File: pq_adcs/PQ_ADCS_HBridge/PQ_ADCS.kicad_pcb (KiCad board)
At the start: 6 copper layers, 40 x 40 mm, 53 parts, among them J1 CES-110-02-L-S, J10 Pico-Clasp_01x09, J11 Pico-Clasp_01x15, J12 CES-102-02-L-S, J2 CES-110-02-L-S, J3 CES-110-02-L-S, J4 CES-110-02-L-S, J5 Pico-Clasp_01x03, J6 Pico-Clasp_01x10, J7 Pico-Clasp_01x10, J8 Pico-Clasp_01x10, J9 Pico-Clasp_01x10, U1 LPV542, U2 LPV542, U3 LPV542, U4 IIM-42652, U5 DRV8214RTER, U6 TMUX1108RSVR, U7 MMC5983MA, U8 DRV8214RTER, U9 DRV8214RTER

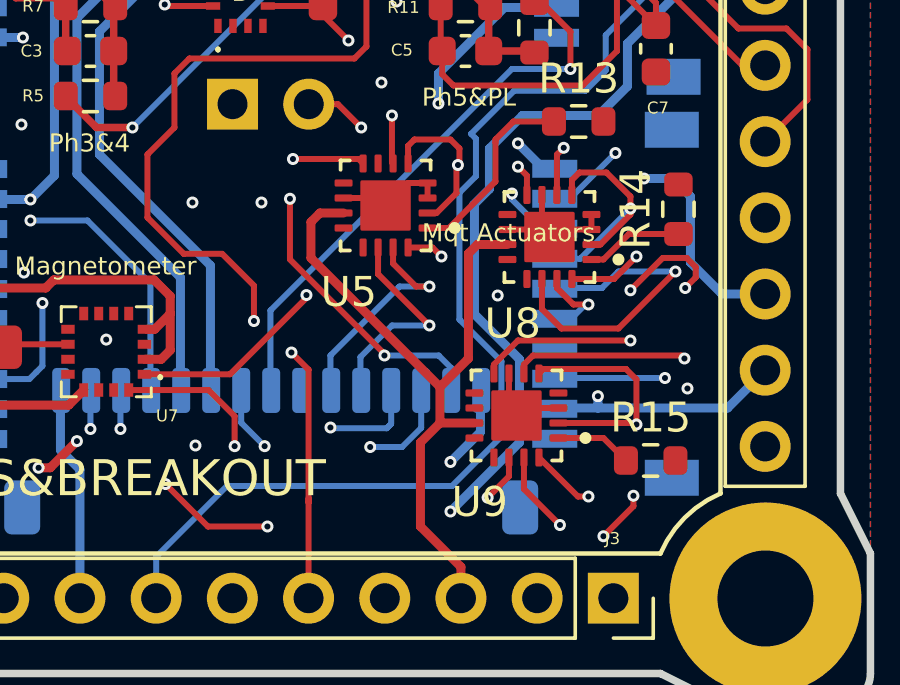
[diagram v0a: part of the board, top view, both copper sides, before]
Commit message: NC digital pincs fix
Unused digital pins as well as I2C pins are now set as not connected instead of grounded. Added lock files to gitignore
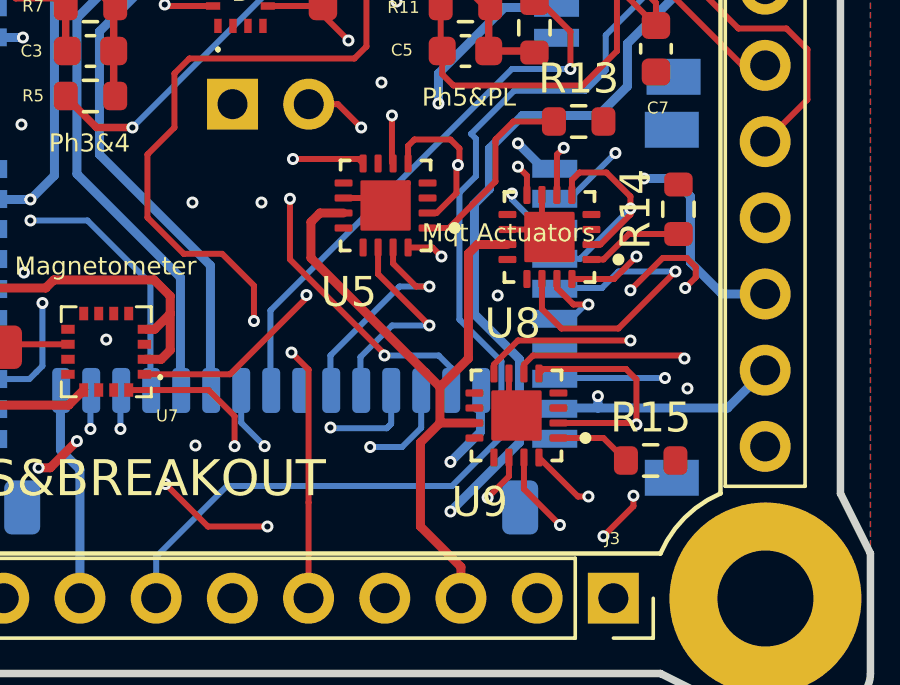
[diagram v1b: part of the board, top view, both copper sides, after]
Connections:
- U5 pad 3: GND -> unconnected-(U5-RC_OUT-Pad3)
- U5 pad 4: GND -> unconnected-(U5-~{FAULT}-Pad4)
- U8 pad 3: GND -> unconnected-(U8-RC_OUT-Pad3)
- U8 pad 4: GND -> unconnected-(U8-~{FAULT}-Pad4)
- U9 pad 3: GND -> unconnected-(U9-RC_OUT-Pad3)
- U9 pad 4: GND -> unconnected-(U9-~{FAULT}-Pad4)
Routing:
- net GND: track 20.2 -> 16.3 mm
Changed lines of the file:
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@@
 	(net 79 "unconnected-(U9-A1-Pad9)")
 	(net 80 "/PHT6_ADCS")
+	(net 81 "unconnected-(U5-~{FAULT}-Pad4)")
+	(net 82 "unconnected-(U5-RC_OUT-Pad3)")
+	(net 83 "unconnected-(U8-RC_OUT-Pad3)")
+	(net 84 "unconnected-(U8-~{FAULT}-Pad4)")
+	(net 85 "unconnected-(U9-RC_OUT-Pad3)")
+	(net 86 "unconnected-(U9-~{FAULT}-Pad4)")
 	(footprint "Resistor_SMD:R_0603_1608Metric"
 		(layer "F.Cu")
@@
 			(layers "F.Cu" "F.Paste")
 			(roundrect_rratio 0.2)
-			(net 1 "GND")
+			(net 82 "unconnected-(U5-RC_OUT-Pad3)")
 			(pinfunction "RC_OUT")
-			(pintype "output")
+			(pintype "output+no_connect")
 		)
 		(pad "4" smd roundrect
@@
 			(layers "F.Cu" "F.Paste")
 			(roundrect_rratio 0.2)
-			(net 1 "GND")
+			(net 81 "unconnected-(U5-~{FAULT}-Pad4)")
 			(pinfunction "~{FAULT}")
-			(pintype "output")
+			(pintype "output+no_connect")
 		)
 		(pad "5" smd roundrect
@@
 			(layers "F.Cu" "F.Paste")
 			(roundrect_rratio 0.2)
-			(net 1 "GND")
+			(net 85 "unconnected-(U9-RC_OUT-Pad3)")
 			(pinfunction "RC_OUT")
-			(pintype "output")
+			(pintype "output+no_connect")
 		)
 		(pad "4" smd roundrect
@@
 			(layers "F.Cu" "F.Paste")
 			(roundrect_rratio 0.2)
-			(net 1 "GND")
+			(net 86 "unconnected-(U9-~{FAULT}-Pad4)")
 			(pinfunction "~{FAULT}")
-			(pintype "output")
+			(pintype "output+no_connect")
 		)
 		(pad "5" smd roundrect
@@
 			(net 79 "unconnected-(U9-A1-Pad9)")
 			(pinfunction "A1")
-			(pintype "input")
+			(pintype "input+no_connect")
 		)
 		(pad "10" smd roundrect
@@
 			(net 78 "unconnected-(U9-A0-Pad10)")
 			(pinfunction "A0")
-			(pintype "input")
+			(pintype "input+no_connect")
 		)
 		(pad "11" smd roundrect
@@
 			(layers "F.Cu" "F.Paste")
 			(roundrect_rratio 0.2)
-			(net 1 "GND")
+			(net 83 "unconnected-(U8-RC_OUT-Pad3)")
 			(pinfunction "RC_OUT")
-			(pintype "output")
+			(pintype "output+no_connect")
 		)
 		(pad "4" smd roundrect
@@
 			(layers "F.Cu" "F.Paste")
 			(roundrect_rratio 0.2)
-			(net 1 "GND")
+			(net 84 "unconnected-(U8-~{FAULT}-Pad4)")
 			(pinfunction "~{FAULT}")
-			(pintype "output")
+			(pintype "output+no_connect")
 		)
 		(pad "5" smd roundrect
@@
 			(net 77 "unconnected-(U8-A1-Pad9)")
 			(pinfunction "A1")
-			(pintype "input")
+			(pintype "input+no_connect")
 		)
 		(pad "10" smd roundrect
@@
 	)
 	(segment
-		(start 160.7 99.2)
-		(end 159.55 99.2)
-		(width 0.2)
-		(layer "F.Cu")
-		(net 1)
-	)
-	(segment
 		(start 144.75 89.5)
 		(end 144 88.75)
@@
 	)
 	(segment
-		(start 159.6 105.15)
-		(end 158.45 105.15)
-		(width 0.2)
-		(layer "F.Cu")
-		(net 1)
-	)
-	(segment
-		(start 155.2375 97.65)
-		(end 154.5875 97.65)
-		(width 0.2)
-		(layer "F.Cu")
-		(net 1)
-	)
-	(segment
 		(start 139 89)
 		(end 138.75 88.75)
@@
 	)
 	(segment
-		(start 155.2375 98.15)
-		(end 155.2375 97.65)
-		(width 0.2)
-		(layer "F.Cu")
-		(net 1)
-	)
-	(segment
 		(start 152.4375 98.15)
 		(end 153.5875 98.15)
@@
 	)
 	(segment
-		(start 160.7 98.7)
-		(end 160.7 99.2)
-		(width 0.2)
-		(layer "F.Cu")
-		(net 1)
-	)
-	(segment
 		(start 159.05 98.05)
 		(end 159.05 99.2)
@@
 		(width 0.2)
 		(layer "F.Cu")
-		(net 26)
-	)
-	(segment
-		(start 151.27 108.155)
-		(end 151.27 108.3)
-		(width 0.2)
-		(layer "F.Cu")

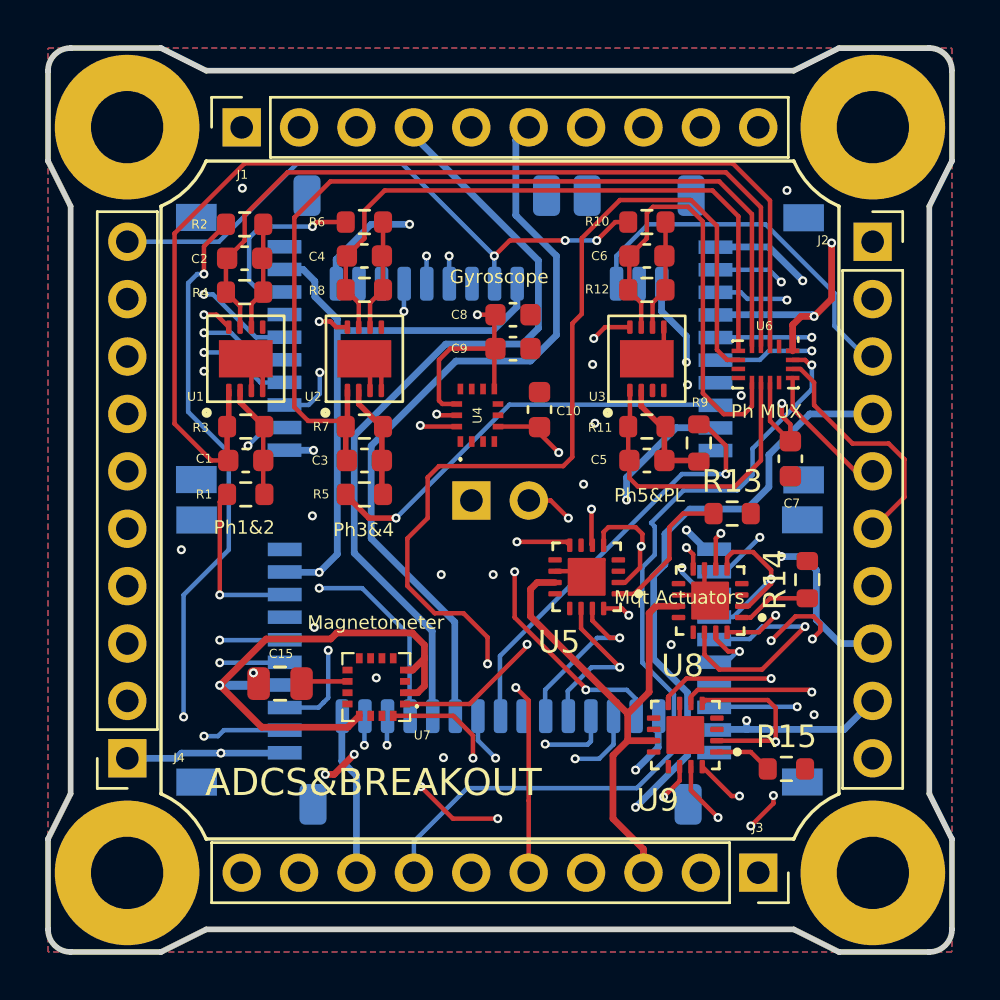
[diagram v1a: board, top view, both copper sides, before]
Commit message: Added Capacitors to HBridge Controllers
Coupling capacitors added as required by the HBridge controllers.
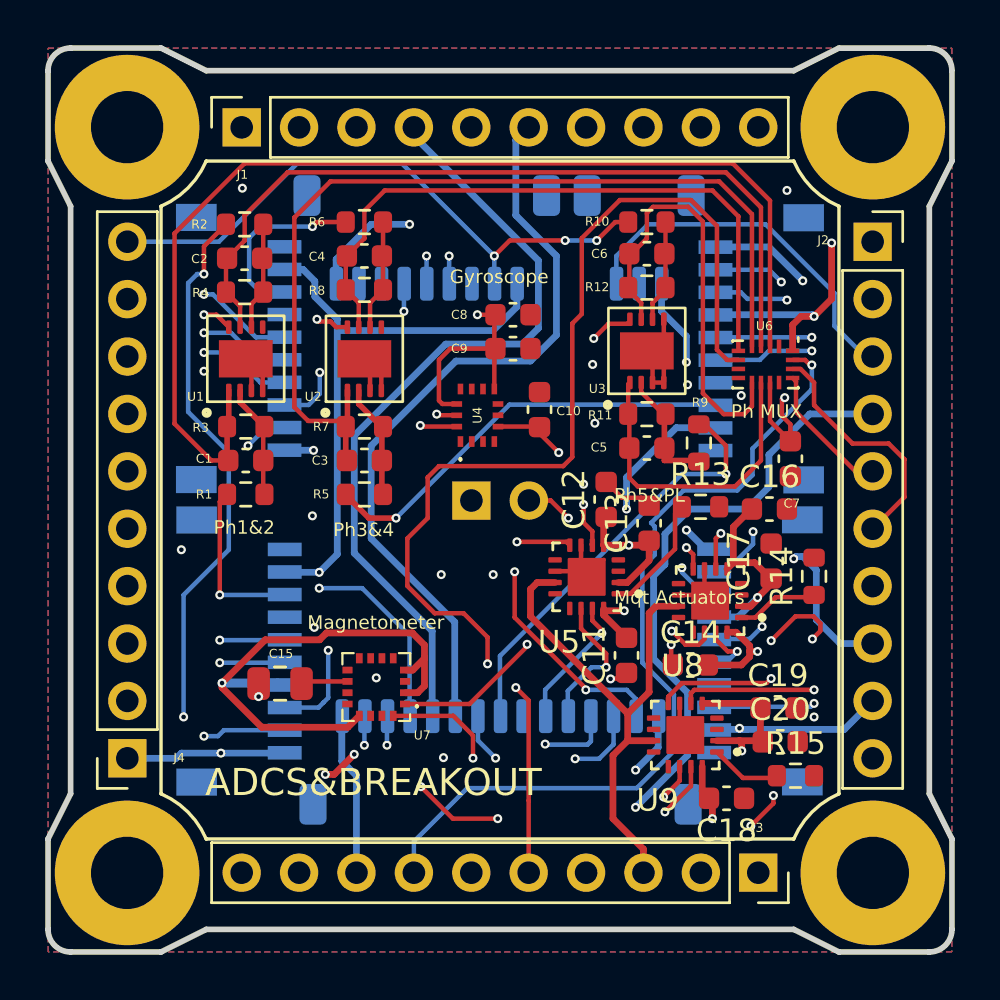
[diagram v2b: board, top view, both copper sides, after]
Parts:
- added C11: 100n, Capacitor_SMD:C_0603_1608Metric, F.Cu at (155.6, 101.9)
- added C12: 100n, Capacitor_SMD:C_0603_1608Metric, F.Cu at (154.7, 95.0)
- added C13: 10u, Capacitor_SMD:C_0603_1608Metric, F.Cu at (156.6, 96.0)
- added C14: 100n, Capacitor_SMD:C_0603_1608Metric, F.Cu at (158.4, 102.3)
- added C16: 100n, Capacitor_SMD:C_0603_1608Metric, F.Cu at (161.9, 95.4)
- added C17: 10u, Capacitor_SMD:C_0603_1608Metric, F.Cu at (162.0, 97.7)
- added C18: 100n, Capacitor_SMD:C_0603_1608Metric, F.Cu at (160.0, 108.2)
- added C19: 100n, Capacitor_SMD:C_0603_1608Metric, F.Cu at (162.3, 104.2)
- added C20: 10u, Capacitor_SMD:C_0603_1608Metric, F.Cu at (162.4, 105.7)
- moved R13 1.43 mm to (158.9, 95.3)
- moved C5 0.55 mm to (156.5, 92.7)
- moved R11 0.55 mm to (156.5, 91.2)
- moved R15 0.50 mm to (163.1, 107.2)
- moved U3 0.35 mm to (156.5, 88.4)
- moved R14 0.34 mm to (163.9, 98.4)
- moved C6 0.10 mm to (156.5, 84.1)
- moved R12 0.10 mm to (156.5, 85.6)
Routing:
- net GND: track 16.3 -> 25.1 mm, vias 18 -> 19
- net SCL3: track 137.5 -> 132.5 mm
- net SDA3: track 151.1 -> 146.3 mm, vias 9 -> 10
- net 3V3_PERM: track 91.4 -> 96.1 mm
- net /PHT2: track 62.8 -> 64.1 mm
- net Net-(U5-IPROPI): track 6.50 -> 5.32 mm
- net /+MAG+Y: track 21.3 -> 20.5 mm
- net Net-(U8-IPROPI): track 3.25 -> 3.89 mm
- net Net-(U9-IPROPI): track 2.56 -> 3.17 mm
- net BURNCOMMS: track 70.4 -> 71.0 mm
- net SWO: track 35.0 -> 35.5 mm
